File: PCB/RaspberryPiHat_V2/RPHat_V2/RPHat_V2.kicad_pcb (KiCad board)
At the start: 2 copper layers, 54 parts, among them IC1 TXB0108YZPR2, J1 Raspberry_Pi_2_3, J10 Conn_01x03, J11 Conn_01x03, J12 Conn_01x03, J13 Conn_01x03, J14 Conn_01x03, J15 Conn_01x01, J16 Conn_01x06, J2 Hall effect connector Right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

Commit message: started pcb routing
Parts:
- IC1: value TXB0108YZPR2 -> TXB0108DQSR; footprint TXB0108YZPR2:BGA20C50P4X5_189X239X50 -> User:TXB0108DQSR
- moved C2 152.9 mm to (212.8, 166.5)
- moved D1 152.9 mm to (212.0, 169.9)
- moved R1 152.9 mm to (212.0, 172.4)
- moved R2 152.9 mm to (216.4, 169.9)
- moved L1 152.9 mm to (218.5, 166.3)
- moved R3 152.9 mm to (220.7, 169.4)
- moved PS1 144.7 mm to (213.2, 149.8)
- moved C1 139.0 mm to (198.0, 166.5)
- moved C3 139.0 mm to (198.0, 170.7)
- moved C4 139.0 mm to (204.0, 166.5)
- moved BT1 130.1 mm to (198.2, 150.0)
- moved J1 125.8 mm to (210.0, 68.0)
- moved J4 113.3 mm to (256.9, 73.4), turned to 270 degrees
- moved U5 110.2 mm to (251.8, 80.6), turned to 90 degrees
- moved C13 103.2 mm to (252.5, 77.1)
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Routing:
- net +3V3: track 0.00 -> 10.2 mm
- net OUTPUT: track 0.00 -> 7.26 mm
- added copper zone on F.Cu, net GNDREF
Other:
- board outline added: 44 x 52.5 mm

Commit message: Continued working on the pcb
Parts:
- added R11: 100k, Resistor_SMD:R_0402_1005Metric_Pad0.72x0.64mm_HandSolder, F.Cu at (202.9, 50.8)
- added R12: 100k, Resistor_SMD:R_0402_1005Metric_Pad0.72x0.64mm_HandSolder, F.Cu at (201.5, 50.8)
- BT1: footprint Connector_PinSocket_2.00mm:PinSocket_1x02_P2.00mm_Vertical -> Connector_AMASS:AMASS_XT60-F_1x02_P7.20mm_Vertical
- C10, C11, C12, C14, C15, C6, C7: footprint Capacitor_SMD:C_0603_1608Metric_Pad1.08x0.95mm_HandSolder -> Capacitor_SMD:C_0402_1005Metric_Pad0.74x0.62mm_HandSolder
- C4: value C -> 10uF
- C5: value C -> 10uF; footprint Capacitor_SMD:C_1206_3216Metric_Pad1.33x1.80mm_HandSolder -> Capacitor_SMD:C_1210_3225Metric_Pad1.33x2.70mm_HandSolder
- J10, J11, J12, J5, J9: footprint Connector_PinHeader_2.54mm:PinHeader_1x03_P2.54mm_Horizontal -> Connector_PinHeader_2.54mm:PinHeader_1x03_P2.54mm_Vertical
- J16: footprint Connector_PinHeader_2.54mm:PinHeader_1x06_P2.54mm_Horizontal -> Connector_PinHeader_2.54mm:PinHeader_1x06_P2.54mm_Vertical
- R7, R8: footprint Resistor_SMD:R_0603_1608Metric_Pad0.98x0.95mm_HandSolder -> Resistor_SMD:R_0402_1005Metric_Pad0.72x0.64mm_HandSolder
- moved L1 149.0 mm to (154.2, 31.9)
- moved C2 145.2 mm to (148.5, 36.4), turned to 270 degrees
- moved C3 141.9 mm to (152.3, 36.4), turned to 270 degrees
- moved C1 140.6 mm to (144.7, 36.4), turned to 270 degrees
- moved R2 139.8 mm to (157.5, 43.2), turned to 270 degrees
- moved C4 138.7 mm to (156.1, 36.3), turned to 270 degrees
- moved D1 138.7 mm to (155.7, 43.2), turned to 270 degrees
- moved R10 124.4 mm to (185.4, 71.1), turned to 180 degrees
- moved PS1 122.0 mm to (166.4, 37.1)
- moved D2 119.9 mm to (185.4, 72.8), turned to 180 degrees
- moved J15 118.2 mm to (139.3, 40.5)
- moved R3 115.6 mm to (163.1, 69.2), turned to 270 degrees
- moved R1 114.9 mm to (161.4, 69.2), turned to 270 degrees
- moved R5 114.7 mm to (145.4, 50.8)
- moved C5 114.4 mm to (175.1, 38.2), turned to 270 degrees
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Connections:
- C14 pad 1: +3V3 -> +1V8
- C15 pad 1: +1V8 -> +3V3
- IC1 pad 13: Net-(IC1-Pad13) -> IMU_INT_18
- IC1 pad 16: +3V3 -> +1V8
- IC1 pad 5: +1V8 -> +3V3
- IC1 pad 6: +1V8 -> +3V3
- IC1 pad 8: Net-(IC1-Pad8) -> IMU_INT_33
- J1 pad 10: GPS_Uart_TX -> GPS_TX
- J1 pad 18: Net-(J1-Pad18) -> IMU_INT_33
- J1 pad 8: GPS_Uart_RX -> GPS_RX
- R8 pad 2: IMU_INT_18 -> IMU_CS_18
- U4 pad 1: (no net) -> GNDREF
- U4 pad 2: (no net) -> GPS_TX
- U4 pad 3: (no net) -> GPS_RX
- U4 pad 4: (no net) -> +5V
- U6 pad 31: Net-(U6-Pad31) -> +3V3
- U6 pad 32: Net-(U6-Pad32) -> GNDREF
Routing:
- net Net-(PS1-PadD1): track 0.00 -> 5.50 mm
- net Net-(C8-Pad2): track 0.00 -> 4.59 mm
- net Net-(C8-Pad1): track 0.00 -> 4.59 mm
- net +BATT: track 0.00 -> 1.79 mm
- net VCC: track 0.00 -> 1.79 mm
- net Net-(D1-Pad2): track 0.00 -> 1.79 mm
- net Net-(D2-Pad1): track 0.00 -> 1.65 mm
- net Net-(D2-Pad2): track 0.00 -> 0.72 mm
- added copper zone on F.Cu, net +5V
- added copper zone on F.Cu, net +BATT
- added copper zone on F.Cu, net Net-(C4-Pad1)
- added copper zone on F.Cu, net VCC
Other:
- board size 44 x 52.5 mm -> 8.2 x 10.5 mm
- rule trace_min: 0.2 -> 0.1524

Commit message: Never gonna give you up
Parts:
- U4: footprint Connector_PinHeader_2.54mm:PinHeader_1x04_P2.54mm_Vertical -> User:GY-NEO6MV2
- moved J11 81.2 mm to (112.2, 196.8)
- moved J2 81.2 mm to (112.7, 175.9)
- moved J3 81.2 mm to (113.8, 191.4)
- moved J10 81.2 mm to (87.6, 215.7)
- moved J12 81.2 mm to (74.2, 215.7)
- moved J13 81.2 mm to (114.4, 216.2)
- moved J14 81.2 mm to (125.6, 206.5)
- moved J5 81.2 mm to (101.0, 216.2)
- moved J6 81.2 mm to (128.4, 216.2)
- moved J7 81.2 mm to (123.7, 216.2)
- moved J8 81.2 mm to (119.1, 216.2)
- moved J9 81.2 mm to (112.2, 206.5)
- moved C6 79.5 mm to (141.9, 116.2), turned to 270 degrees
- moved C7 78.0 mm to (143.6, 116.2), turned to 270 degrees
- moved U1 72.9 mm to (143.2, 113.1), turned to 0 degrees
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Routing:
- net SPI_MISO_18: track 0.00 -> 21.9 mm, vias 0 -> 2
- net SPI_MOSI_18: track 0.00 -> 16.5 mm, vias 0 -> 2
- net SPI_CLK_18: track 0.00 -> 15.6 mm, vias 0 -> 2
- net IMU_CS_18: track 0.00 -> 13.5 mm, vias 0 -> 2
- net BME_CS_18: track 0.00 -> 10.7 mm
- net +1V8: track 0.00 -> 7.87 mm
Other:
- copper layers 2 -> 4
- rule via_min_drill: 0.3 -> 0.2

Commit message: working on pcb Ja!
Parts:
- removed J10, J9: Conn_01x03, Connector_PinHeader_2.54mm:PinHeader_1x03_P2.54mm_Vertical
- J11, J12, J13, J14, J5, J6, J7, J8: footprint Connector_PinHeader_2.54mm:PinHeader_1x03_P2.54mm_Vertical -> Connector_JST:JST_EH_B3B-EH-A_1x03_P2.50mm_Vertical
- J16: footprint Connector_PinHeader_2.54mm:PinHeader_1x06_P2.54mm_Vertical -> Connector_JST:JST_EH_B6B-EH-A_1x06_P2.50mm_Vertical
- moved J12 121.3 mm to (156.7, 126.7), turned to 90 degrees
- moved J13 80.8 mm to (143.7, 140.9), turned to 270 degrees
- moved J3 78.8 mm to (127.8, 113.8), turned to 90 degrees
- moved J5 78.3 mm to (122.7, 140.9), turned to 270 degrees
- moved J8 77.7 mm to (138.4, 140.9), turned to 270 degrees
- moved J7 75.9 mm to (133.1, 140.9), turned to 270 degrees
- moved J6 75.3 mm to (127.8, 140.9), turned to 270 degrees
- moved U5 74.1 mm to (195.6, 129.0)
- moved C13 74.1 mm to (196.4, 125.5)
- moved J4 74.1 mm to (200.8, 121.8)
- moved R9 74.1 mm to (199.9, 125.5)
- moved J11 73.3 mm to (156.7, 138.5), turned to 90 degrees
- moved J14 69.7 mm to (149.1, 140.9), turned to 270 degrees
- moved J2 65.4 mm to (133.4, 113.8), turned to 90 degrees
- moved SW1 42.5 mm to (109.2, 116.8), turned to 0 degrees
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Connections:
- IC1 pad 1: SPI_MOSI_33 -> SPI_MISO_33
- IC1 pad 19: SPI_MISO_18 -> SPI_MOSI_18
- IC1 pad 2: SPI_MISO_33 -> SPI_MOSI_33
- IC1 pad 20: SPI_MOSI_18 -> SPI_MISO_18
- J16 pad 4: PWM_Left_1 -> PWM_Left_2
- U6 pad 27: Net-(U6-Pad27) -> HE_R_OUTPUT
- U6 pad 28: Net-(U6-Pad28) -> HE_L_OUTPUT
- U6 pad 7: PWM_Left_1 -> PWM_Left_2
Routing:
- net IMU_INT_18: track 0.00 -> 15.5 mm
- net IMU_CS_33: track 0.00 -> 5.97 mm
- net BME_CS_33: track 0.00 -> 4.59 mm
- net +1V8: track 7.87 -> 11.6 mm
- net SPI_MISO_18: track 21.9 -> 19.0 mm
- net SPI_MOSI_18: track 16.5 -> 15.8 mm
- net SPI_CLK_18: track 15.6 -> 15.0 mm
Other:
- board size 8.2 x 10.5 mm -> 109.9 x 62.2 mm

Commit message: pcb update
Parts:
- moved J16 5.82 mm to (101.1, 140.0)
- moved C2 0.92 mm to (106.2, 94.6)
- moved C3 0.92 mm to (110.0, 94.6)
- moved C8 0.92 mm to (105.8, 108.1)
- moved C9 0.92 mm to (105.5, 104.2)
- moved BT1 0.92 mm to (97.1, 120.5)
- moved C1 0.92 mm to (102.4, 94.6)
- moved C4 0.92 mm to (113.8, 94.6)
- moved D1 0.92 mm to (113.5, 101.4)
- moved J15 0.92 mm to (97.1, 98.8)
- moved L1 0.92 mm to (111.9, 90.1)
- moved PS1 0.92 mm to (124.1, 95.3)
- moved R2 0.92 mm to (115.2, 101.4)
- moved R4 0.92 mm to (97.1, 108.4)
- moved R5 0.92 mm to (103.2, 109.0)
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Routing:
- net SCL: track 0.00 -> 81.7 mm
- net SDA: track 0.00 -> 81.4 mm
- net GPS_TX: track 0.00 -> 22.0 mm
- net GPS_RX: track 0.00 -> 18.4 mm
- net +3V3: track 10.2 -> 12.8 mm
- net Net-(D2-Pad1): track 1.65 -> 0.00 mm
- net Net-(D2-Pad2): track 0.72 -> 0.00 mm
- added copper zone on In1.Cu, net GNDREF
- added copper zone on In2.Cu, net GNDREF
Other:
- outline, holes or cut-outs redrawn

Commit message: Work, work, work
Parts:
- added C16: 4,7uF, Capacitor_SMD:C_0402_1005Metric_Pad0.74x0.62mm_HandSolder, F.Cu at (149.4, 105.3)
- added C17: 1uF, Capacitor_SMD:C_0402_1005Metric_Pad0.74x0.62mm_HandSolder, F.Cu at (154.9, 105.3)
- added U7: TPS78418QWDRBRQ1, Package_SON:Texas_S-PVSON-N8_ThermalVias, F.Cu at (152.1, 106.6)
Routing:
- net +5V: track 0.00 -> 170.7 mm, vias 0 -> 4
- net +3V3: track 12.8 -> 123.5 mm, vias 0 -> 4
- net +1V8: track 11.6 -> 44.2 mm, vias 0 -> 5
- net PWM_Left_2: track 0.00 -> 27.0 mm
- net Neopixels_1: track 0.00 -> 27.0 mm
- net PWM_Right_2: track 0.00 -> 26.9 mm
- net PWM_Left_1: track 0.00 -> 26.8 mm
- net PWM_Right_1: track 0.00 -> 26.8 mm
- net Neopixels_2: track 0.00 -> 18.7 mm
- net PWMservo_1: track 0.00 -> 15.7 mm
- net PWMservo_2: track 0.00 -> 13.6 mm
- net SPI_MISO_33: track 0.00 -> 12.4 mm
- net SPI_CLK_33: track 0.00 -> 12.3 mm
- net SPI_MOSI_33: track 0.00 -> 12.2 mm
- net IMU_INT_33: track 0.00 -> 11.1 mm
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- added copper zone on In2.Cu, net +5V
- added copper zone on B.Cu, net GNDREF

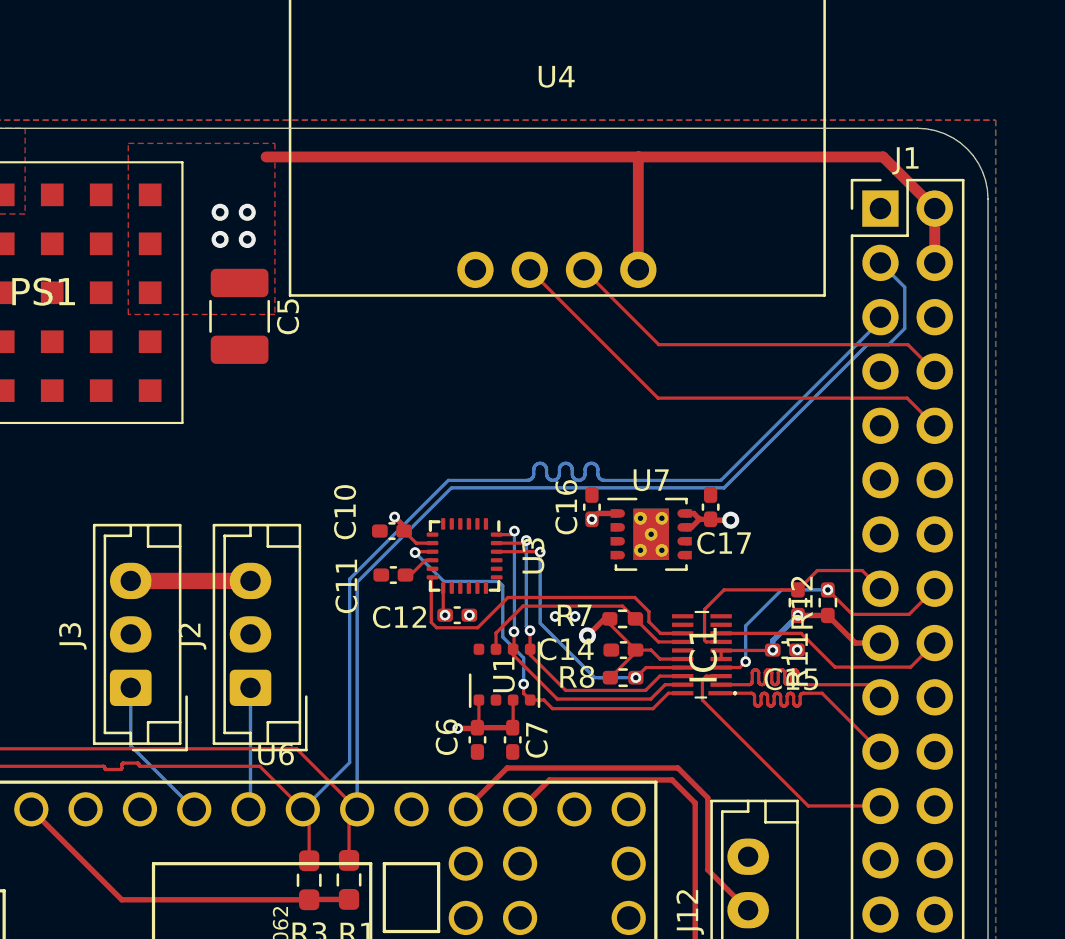
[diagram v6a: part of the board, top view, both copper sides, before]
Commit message: PCB done. only a few grounding vias left to add
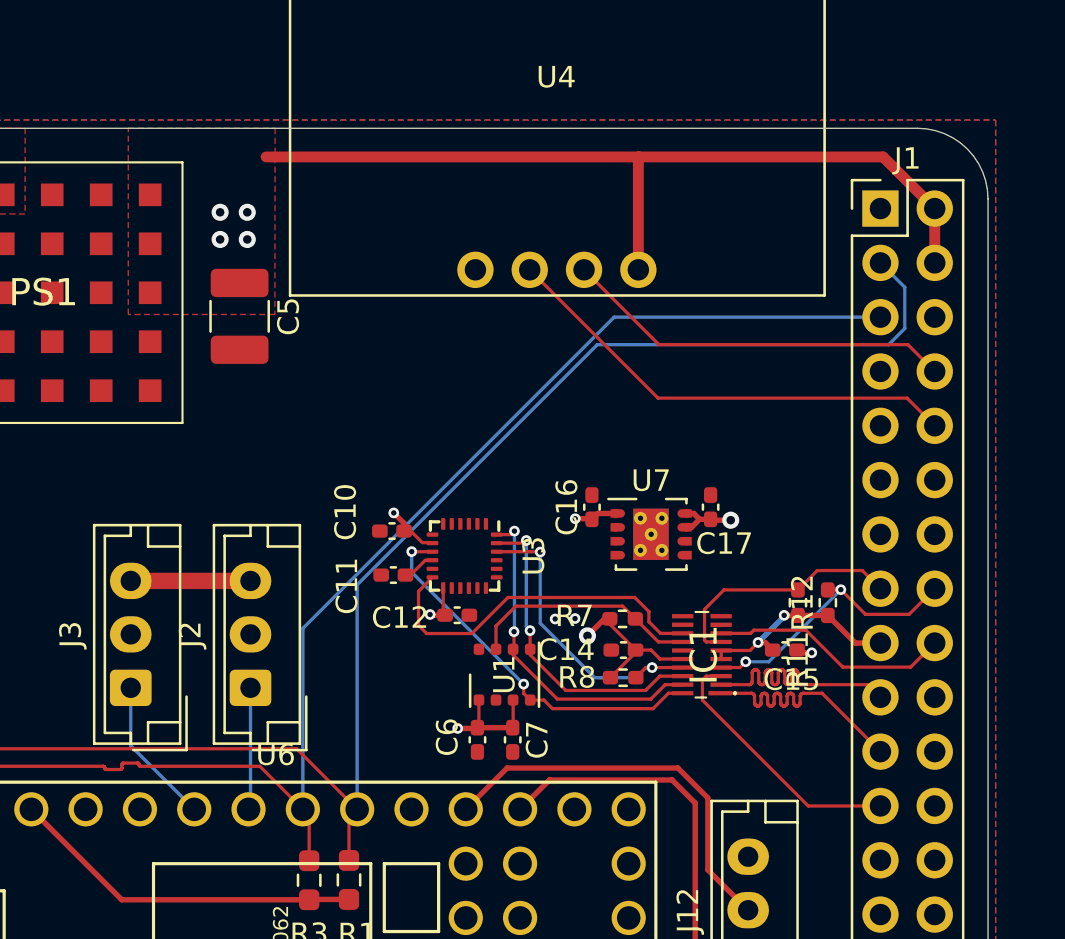
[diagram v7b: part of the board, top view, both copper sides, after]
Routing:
- net SCL: track 82.0 -> 78.6 mm
- net SPI_MISO_18: track 19.0 -> 17.8 mm
- net IMU_INT_18: track 15.5 -> 16.7 mm
- net IMU_CS_18: track 13.6 -> 14.6 mm
- net GNDREF: track 0.00 -> 0.74 mm, vias 4 -> 3
- net +3V3: track 123.5 -> 124.1 mm

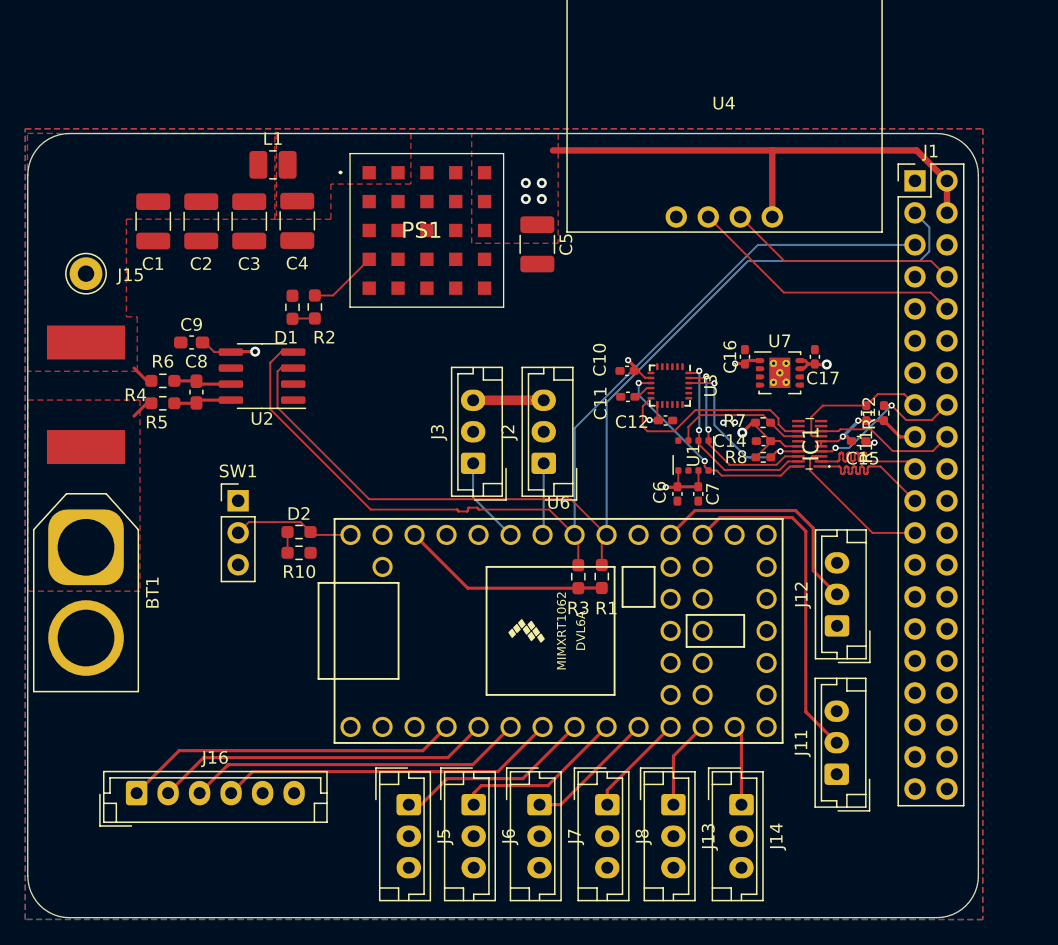
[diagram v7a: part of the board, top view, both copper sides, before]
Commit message: retraced as well as added ground vias
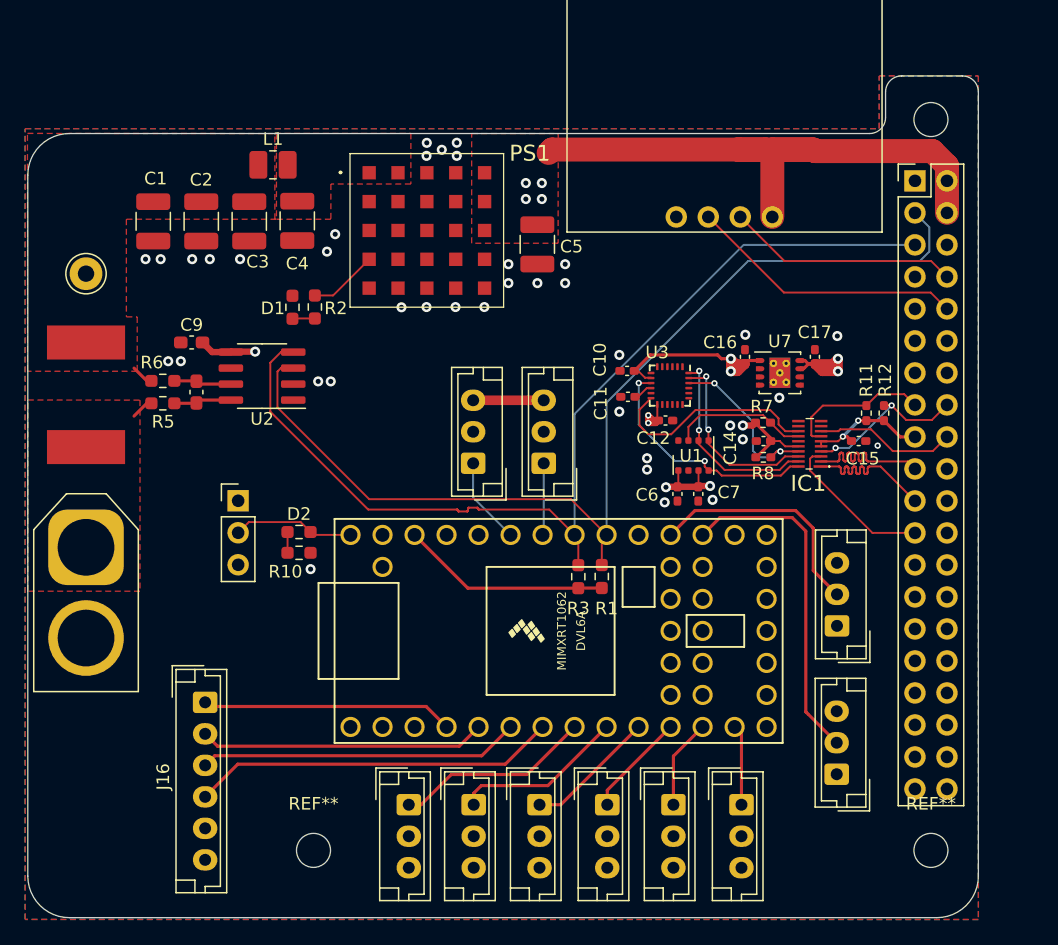
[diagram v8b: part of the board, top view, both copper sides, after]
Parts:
- added REF**: MountingHole_2.7mm_M2.5, MountingHole:MountingHole_2.7mm_M2.5, F.Cu at (115.1, 144.5)
- added REF**: MountingHole_2.7mm_M2.5, MountingHole:MountingHole_2.7mm_M2.5, F.Cu at (164.1, 144.5)
- added REF**: MountingHole_2.7mm_M2.5, MountingHole:MountingHole_2.7mm_M2.5, F.Cu at (164.1, 86.5)
- moved J16 9.03 mm to (106.5, 132.8), turned to 270 degrees
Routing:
- net +1V8: track 44.3 -> 59.9 mm, vias 5 -> 8
- net +3V3: track 124.1 -> 134.3 mm, vias 4 -> 5
- net PWM_Right_1: track 26.8 -> 20.0 mm
- net +5V: track 170.7 -> 177.1 mm
- net PWM_Left_1: track 26.8 -> 22.7 mm
- net PWM_Left_2: track 27.0 -> 29.1 mm
- net SPI_MISO_18: track 17.8 -> 19.2 mm
- net PWM_Right_2: track 26.9 -> 25.5 mm
- net IMU_CS_18: track 14.6 -> 13.6 mm
- net SCL: track 78.6 -> 79.4 mm
- net GNDREF: track 0.74 -> 0.00 mm, vias 3 -> 37
- net IMU_INT_18: track 16.7 -> 17.2 mm
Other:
- board size 109.9 x 62.2 mm -> 109.9 x 66.8 mm
